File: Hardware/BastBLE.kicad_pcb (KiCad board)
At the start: 2 copper layers, 50.8 x 22.9 mm, 41 parts, among them J1 Conn_Battery, J2 SWD, J3 Conn_left, J4 Conn_right, P1 USB_C_Plug_USB2.0, Q1 DMG3415U-7, SW1 RESET, U1 AP2112K-3.3, U2 E73-2G4M08S1C, U3 MCP73831-2-OT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

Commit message: C6 VBUS
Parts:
- C6: moved to B.Cu
- moved C6 17.0 mm to (165.9, 98.6), turned to 180 degrees
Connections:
- C6 pad 1: +3V3 -> VBUS
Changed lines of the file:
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@@
     (solder_mask_min_width 0.25)
     (aux_axis_origin 0 0)
-    (visible_elements 7FFFF7FF)
+    (visible_elements 7FFFFFFF)
     (pcbplotparams
       (layerselection 0x010fc_ffffffff)
@@
     )
   )
-  (module Capacitor_SMD:C_0603_1608Metric_Pad1.05x0.95mm_HandSolder (layer F.Cu)
-    (at 152.73 87.865 90)
+  (module Capacitor_SMD:C_0603_1608Metric_Pad1.05x0.95mm_HandSolder (layer B.Cu)
+    (at 165.88 98.56 180)
     (descr "Capacitor SMD 0603 (1608 Metric), square (rectangular) end terminal, IPC_7351 nominal with elongated pad for handsoldering. (Body size source: http://www.tortai-tech.com/upload/download/2011102023233369053.pdf), generated with kicad-footprint-generator")
     (tags "capacitor handsolder")
     (attr smd)
-    (fp_text reference C6 (at 2.785 0 90) (layer F.SilkS)
-      (effects (font (size 1 1) (thickness 0.15)))
-    )
-    (fp_text value 0.1uF (at 0 1.43 90) (layer F.Fab)
-      (effects (font (size 1 1) (thickness 0.15)))
-    )
-    (fp_line (start -0.8 0.4) (end -0.8 -0.4) (layer F.Fab) (width 0.1))
-    (fp_line (start -0.8 -0.4) (end 0.8 -0.4) (layer F.Fab) (width 0.1))
-    (fp_line (start 0.8 -0.4) (end 0.8 0.4) (layer F.Fab) (width 0.1))
-    (fp_line (start 0.8 0.4) (end -0.8 0.4) (layer F.Fab) (width 0.1))
-    (fp_line (start -0.171267 -0.51) (end 0.171267 -0.51) (layer F.SilkS) (width 0.12))
-    (fp_line (start -0.171267 0.51) (end 0.171267 0.51) (layer F.SilkS) (width 0.12))
-    (fp_line (start -1.65 0.73) (end -1.65 -0.73) (layer F.CrtYd) (width 0.05))
-    (fp_line (start -1.65 -0.73) (end 1.65 -0.73) (layer F.CrtYd) (width 0.05))
-    (fp_line (start 1.65 -0.73) (end 1.65 0.73) (layer F.CrtYd) (width 0.05))
-    (fp_line (start 1.65 0.73) (end -1.65 0.73) (layer F.CrtYd) (width 0.05))
-    (fp_text user %R (at 0 0 90) (layer F.Fab)
-      (effects (font (size 0.4 0.4) (thickness 0.06)))
-    )
-    (pad 1 smd roundrect (at -0.875 0 90) (size 1.05 0.95) (layers F.Cu F.Paste F.Mask) (roundrect_rratio 0.25)
-      (net 15 +3V3))
-    (pad 2 smd roundrect (at 0.875 0 90) (size 1.05 0.95) (layers F.Cu F.Paste F.Mask) (roundrect_rratio 0.25)
+    (fp_text reference C6 (at 2.785 0) (layer B.SilkS)
+      (effects (font (size 1 1) (thickness 0.15)) (justify mirror))
+    )
+    (fp_text value 0.1uF (at 0 -1.43) (layer B.Fab)
+      (effects (font (size 1 1) (thickness 0.15)) (justify mirror))
+    )
+    (fp_line (start -0.8 -0.4) (end -0.8 0.4) (layer B.Fab) (width 0.1))
+    (fp_line (start -0.8 0.4) (end 0.8 0.4) (layer B.Fab) (width 0.1))
+    (fp_line (start 0.8 0.4) (end 0.8 -0.4) (layer B.Fab) (width 0.1))
+    (fp_line (start 0.8 -0.4) (end -0.8 -0.4) (layer B.Fab) (width 0.1))
+    (fp_line (start -0.171267 0.51) (end 0.171267 0.51) (layer B.SilkS) (width 0.12))
+    (fp_line (start -0.171267 -0.51) (end 0.171267 -0.51) (layer B.SilkS) (width 0.12))
+    (fp_line (start -1.65 -0.73) (end -1.65 0.73) (layer B.CrtYd) (width 0.05))
+    (fp_line (start -1.65 0.73) (end 1.65 0.73) (layer B.CrtYd) (width 0.05))
+    (fp_line (start 1.65 0.73) (end 1.65 -0.73) (layer B.CrtYd) (width 0.05))
+    (fp_line (start 1.65 -0.73) (end -1.65 -0.73) (layer B.CrtYd) (width 0.05))
+    (fp_text user %R (at 0 0) (layer B.Fab)
+      (effects (font (size 0.4 0.4) (thickness 0.06)) (justify mirror))
+    )
+    (pad 1 smd roundrect (at -0.875 0 180) (size 1.05 0.95) (layers B.Cu B.Paste B.Mask) (roundrect_rratio 0.25)
+      (net 3 VBUS))
+    (pad 2 smd roundrect (at 0.875 0 180) (size 1.05 0.95) (layers B.Cu B.Paste B.Mask) (roundrect_rratio 0.25)
       (net 2 GND))
     (model ${KISYS3DMOD}/Capacitor_SMD.3dshapes/C_0603_1608Metric.wrl

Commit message: D- D+
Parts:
- moved U4 20.4 mm to (172.1, 91.7)
- moved J2 4.57 mm to (157.3, 92.3), turned to 90 degrees
- moved Q1 4.39 mm to (144.9, 90.2)
- moved R5 4.10 mm to (148.5, 91.2)
- moved D2 4.10 mm to (152.2, 86.6)
- moved R4 4.10 mm to (152.2, 88.3)
- moved U1 4.10 mm to (148.6, 86.9)
- moved R6 4.10 mm to (148.5, 89.6)
- moved D1 2.49 mm to (141.2, 92.5), turned to 270 degrees
- moved C3 2.17 mm to (149.3, 93.7)
- moved R3 1.00 mm to (144.1, 99.0)
- moved U3 0.95 mm to (144.3, 96.4)
- moved C2 0.29 mm to (141.5, 97.6)
- moved C7 0.29 mm to (139.1, 99.7)
- moved C1 0.29 mm to (139.1, 96.7)
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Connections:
- U2 pad 1: /D5 -> /SCK
- U2 pad 14: /D12 -> /D6
- U2 pad 16: /D6 -> /D12
- U2 pad 17: /D9 -> /D11
- U2 pad 18: /D11 -> /D9
- U2 pad 6: /SCK -> /D5
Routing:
- net /D+: track 3.46 -> 46.4 mm, vias 0 -> 2
- net /D-: track 3.56 -> 44.4 mm, vias 0 -> 2
- net VBUS: track 0.00 -> 37.4 mm, vias 0 -> 2
- net /SWCLK: track 0.00 -> 30.8 mm, vias 0 -> 1
- net /SWDIO: track 0.00 -> 27.2 mm, vias 0 -> 1
- net /MOSI: track 0.00 -> 18.9 mm
- net Net-(C1-Pad1): track 0.00 -> 15.6 mm, vias 0 -> 2
- net /MISO: track 0.00 -> 13.2 mm, vias 0 -> 1
- net /RX: track 0.00 -> 11.3 mm
- net /TX: track 0.00 -> 10.0 mm
- net +3V3: track 0.00 -> 7.80 mm
- net Net-(P1-PadA5): track 1.87 -> 5.61 mm

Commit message: Flash memory
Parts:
- moved U4 0.48 mm to (172.0, 91.2), turned to 180 degrees
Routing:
- net /QSPI_SCK: track 0.00 -> 21.7 mm, vias 0 -> 5
- net +3V3: track 7.80 -> 21.6 mm, vias 0 -> 1
- net /SDA: track 0.00 -> 11.1 mm, vias 0 -> 1
- net /QSPI_CS: track 0.00 -> 9.88 mm
- net /QSPI_DATA1: track 0.00 -> 8.20 mm
- net /QSPI_DATA2: track 0.17 -> 7.43 mm
- net /QSPI_DATA3: track 0.00 -> 5.04 mm
- net /QSPI_DATA0: track 0.00 -> 3.48 mm
- net /MISO: track 13.2 -> 12.1 mm

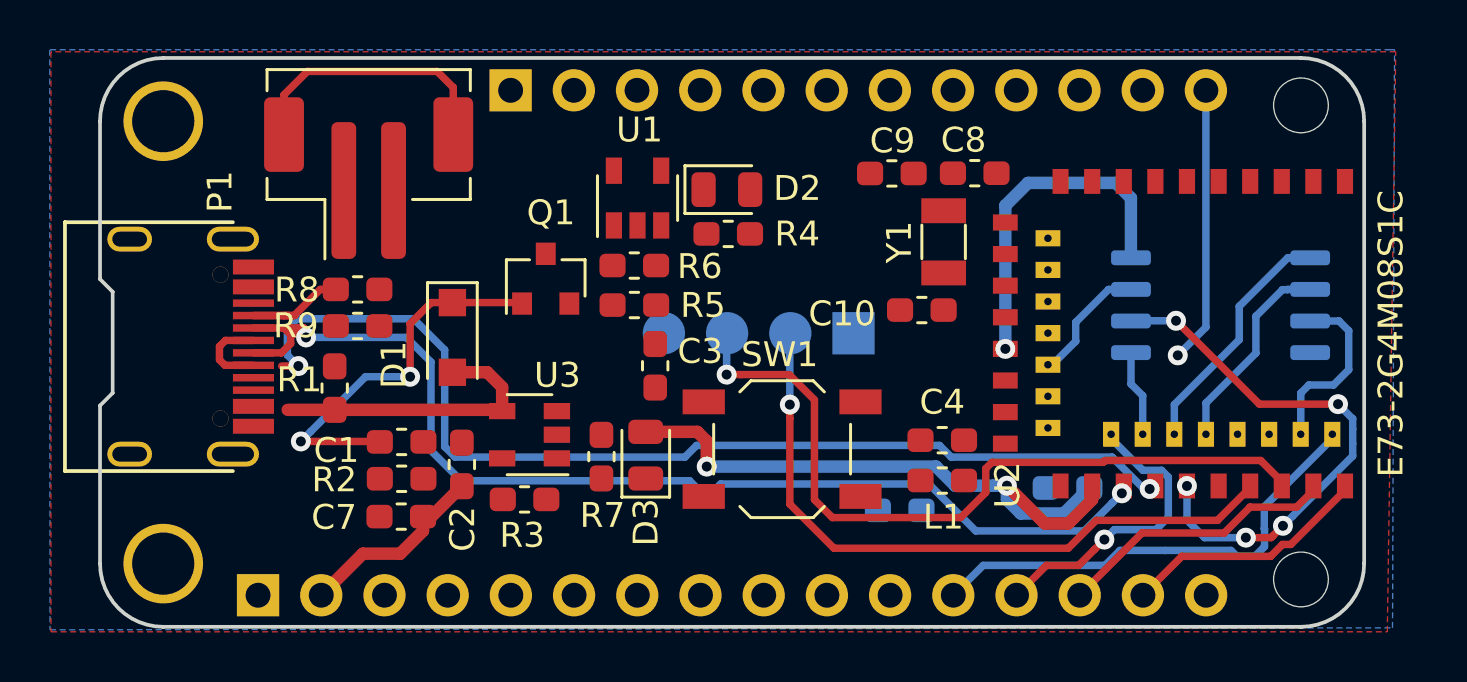
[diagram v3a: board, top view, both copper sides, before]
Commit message: change pin SDA SCL
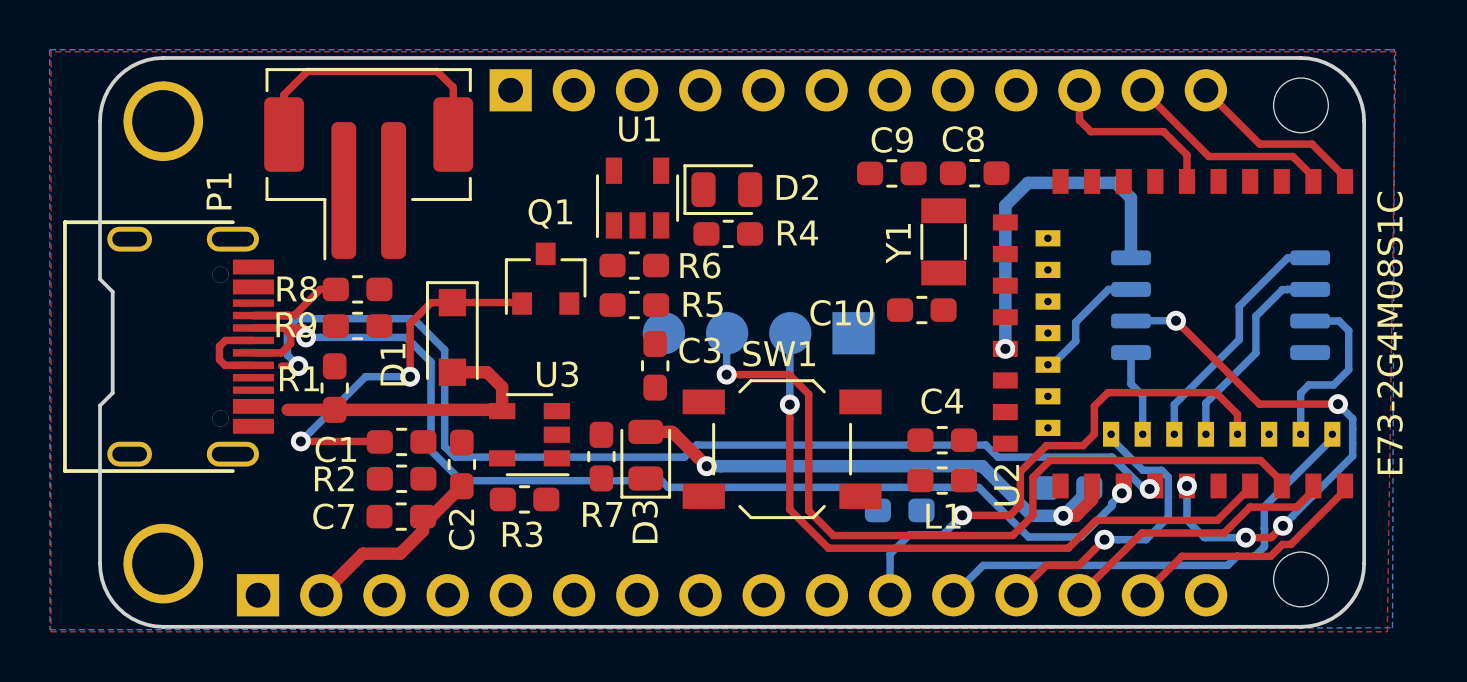
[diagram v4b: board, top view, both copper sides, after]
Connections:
- U2 pad 1: /SCK -> /SDA
- U2 pad 2: /LED -> /SCL
- U2 pad 35: /SDA -> /LED
- U2 pad 36: /SCL -> /SCK
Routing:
- net /SCK: track 0.00 -> 20.9 mm, vias 0 -> 1
- net /SCL: track 0.00 -> 8.48 mm
- net /D5: track 0.00 -> 7.16 mm
- net /SDA: track 11.1 -> 7.21 mm, vias 1 -> 0
- net VBUS: track 37.4 -> 33.6 mm
- net /SWCLK: track 30.8 -> 32.1 mm

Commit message: fix components
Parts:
- moved Q1 0.07 mm to (144.9, 90.2), turned to 270 degrees
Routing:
- net /D10: track 0.00 -> 27.3 mm, vias 0 -> 1
- net +BATT: track 0.00 -> 12.7 mm
- net /D6: track 0.00 -> 12.6 mm
- net /QSPI_SCK: track 21.7 -> 29.9 mm
- net /EN: track 0.00 -> 7.59 mm
- net Net-(C1-Pad1): track 15.6 -> 22.6 mm
- net Net-(C10-Pad1): track 0.00 -> 4.29 mm
- net Net-(C9-Pad1): track 0.00 -> 2.68 mm
- net Net-(R7-Pad2): track 0.00 -> 2.18 mm
- net Net-(D2-Pad2): track 0.00 -> 1.78 mm
- net Net-(D3-Pad1): track 0.00 -> 1.78 mm
- net Net-(R3-Pad1): track 0.00 -> 1.66 mm
- net /VBAT: track 0.00 -> 1.59 mm
- net /QSPI_DATA3: track 5.04 -> 5.83 mm

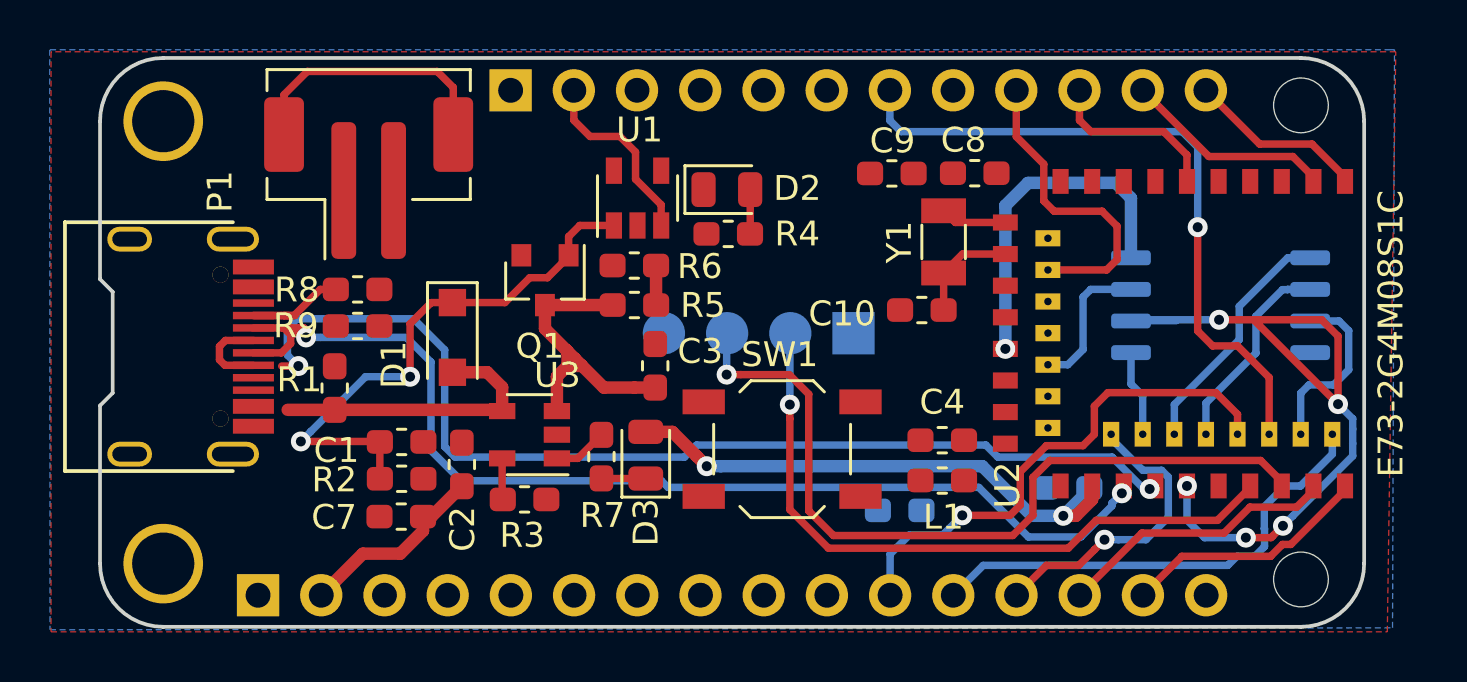
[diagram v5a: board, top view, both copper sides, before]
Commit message: fix traces
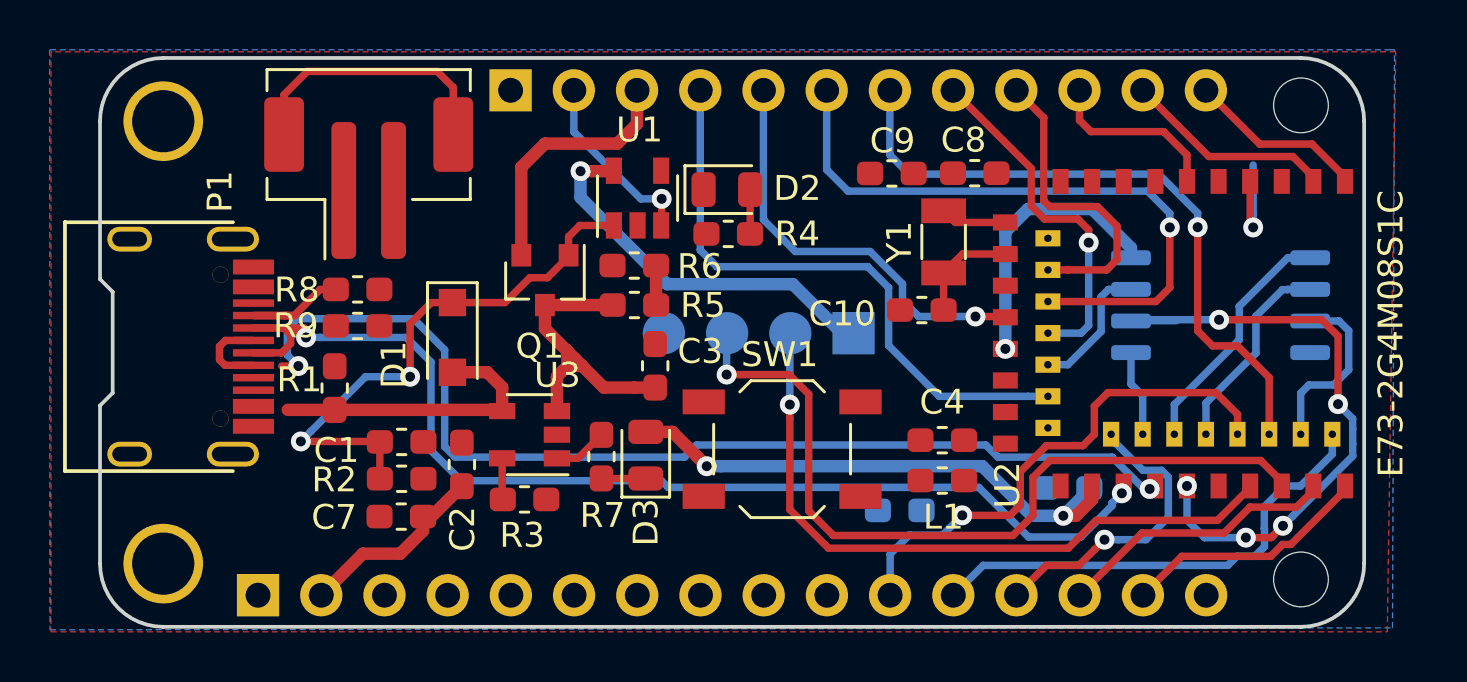
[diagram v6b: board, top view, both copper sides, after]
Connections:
- U2 pad 16: /D12 -> /D11
- U2 pad 17: /D11 -> /D12
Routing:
- net /D11: track 0.00 -> 25.8 mm, vias 0 -> 1
- net /D13: track 0.00 -> 24.2 mm
- net /D12: track 0.00 -> 16.9 mm, vias 0 -> 1
- net /D9: track 0.00 -> 14.3 mm, vias 0 -> 1
- net +3V3: track 21.6 -> 34.6 mm, vias 1 -> 2
- net VBUS: track 33.6 -> 43.8 mm
- net /QSPI_SCK: track 29.9 -> 25.2 mm
- net /A4: track 0.00 -> 4.41 mm, vias 0 -> 1
- net /D10: track 27.3 -> 26.6 mm
- net /EN: track 7.59 -> 7.39 mm, vias 0 -> 1

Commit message: tracks u2
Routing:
- net /A1: track 0.00 -> 50.9 mm, vias 0 -> 3
- net /A0: track 0.00 -> 45.0 mm, vias 0 -> 4
- net /A4: track 4.41 -> 40.3 mm, vias 1 -> 3
- net /AREF: track 0.00 -> 4.72 mm, vias 0 -> 2
- net /D11: track 25.8 -> 29.7 mm
- net /QSPI_SCK: track 25.2 -> 23.4 mm
- net /SWDIO: track 27.3 -> 28.7 mm
- net /SWCLK: track 32.1 -> 32.9 mm
- net /D10: track 26.6 -> 26.0 mm

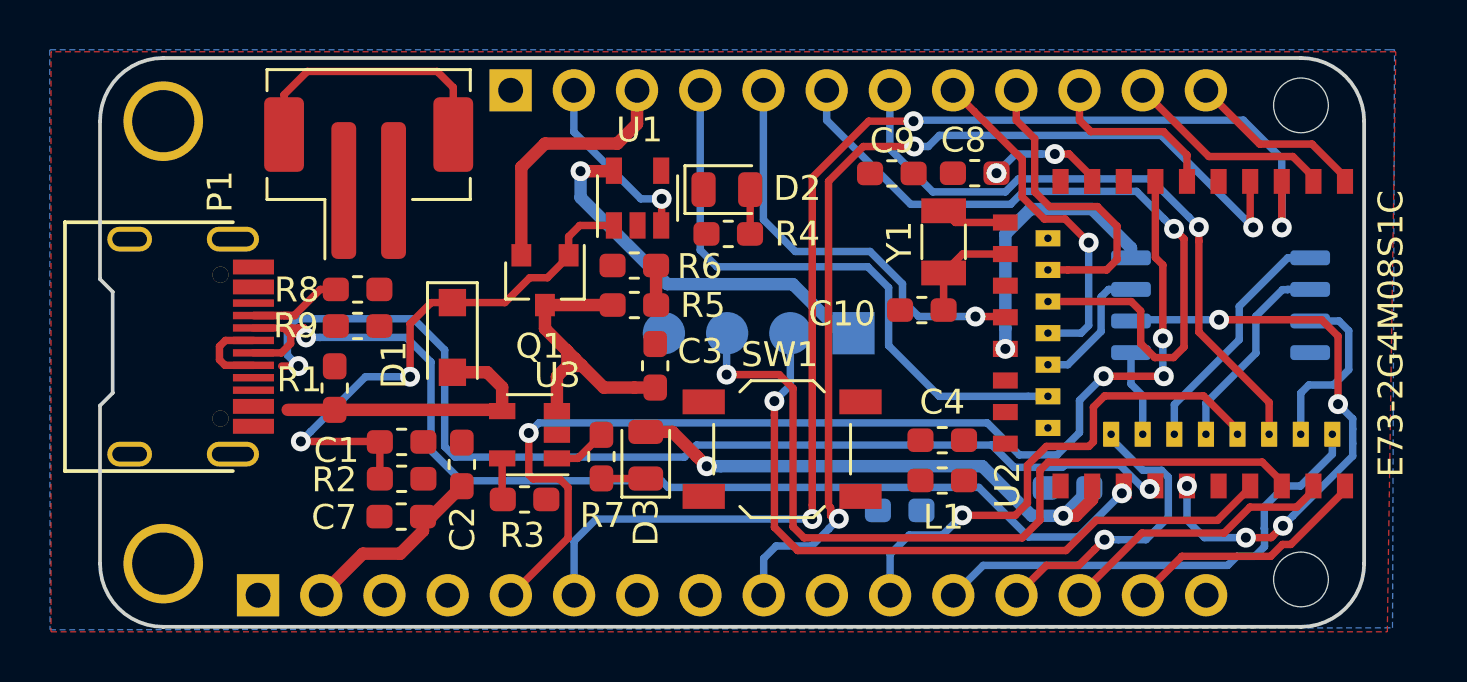
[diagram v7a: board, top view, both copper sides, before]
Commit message: VBUS and batt
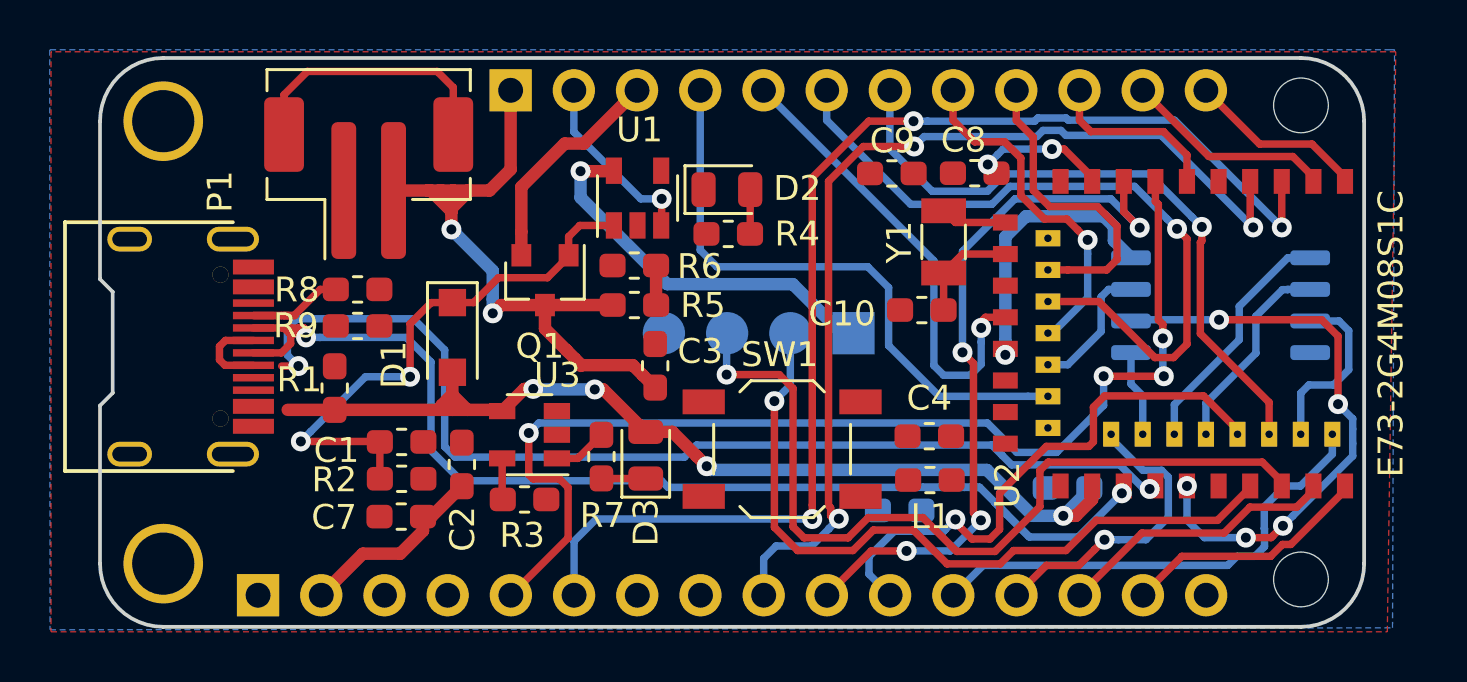
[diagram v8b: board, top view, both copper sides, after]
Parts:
- moved C4 0.54 mm to (160.3, 96.5)
- moved L1 0.50 mm to (160.3, 98.2)
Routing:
- net /A5: track 0.00 -> 29.2 mm, vias 0 -> 4
- net +BATT: track 12.7 -> 30.0 mm, vias 0 -> 2
- net VBUS: track 43.8 -> 49.4 mm, vias 2 -> 4
- net /D-: track 44.5 -> 49.0 mm
- net /D12: track 16.9 -> 18.9 mm
- net /SCK: track 20.7 -> 22.5 mm
- net /A1: track 50.9 -> 49.4 mm
- net /SWDIO: track 28.7 -> 29.8 mm
- net /SWCLK: track 32.9 -> 33.7 mm
